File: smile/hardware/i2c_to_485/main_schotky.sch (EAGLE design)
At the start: 12 parts, among them IC1 MAX481CSA, IC2 MAX481CSA, U1 7402D

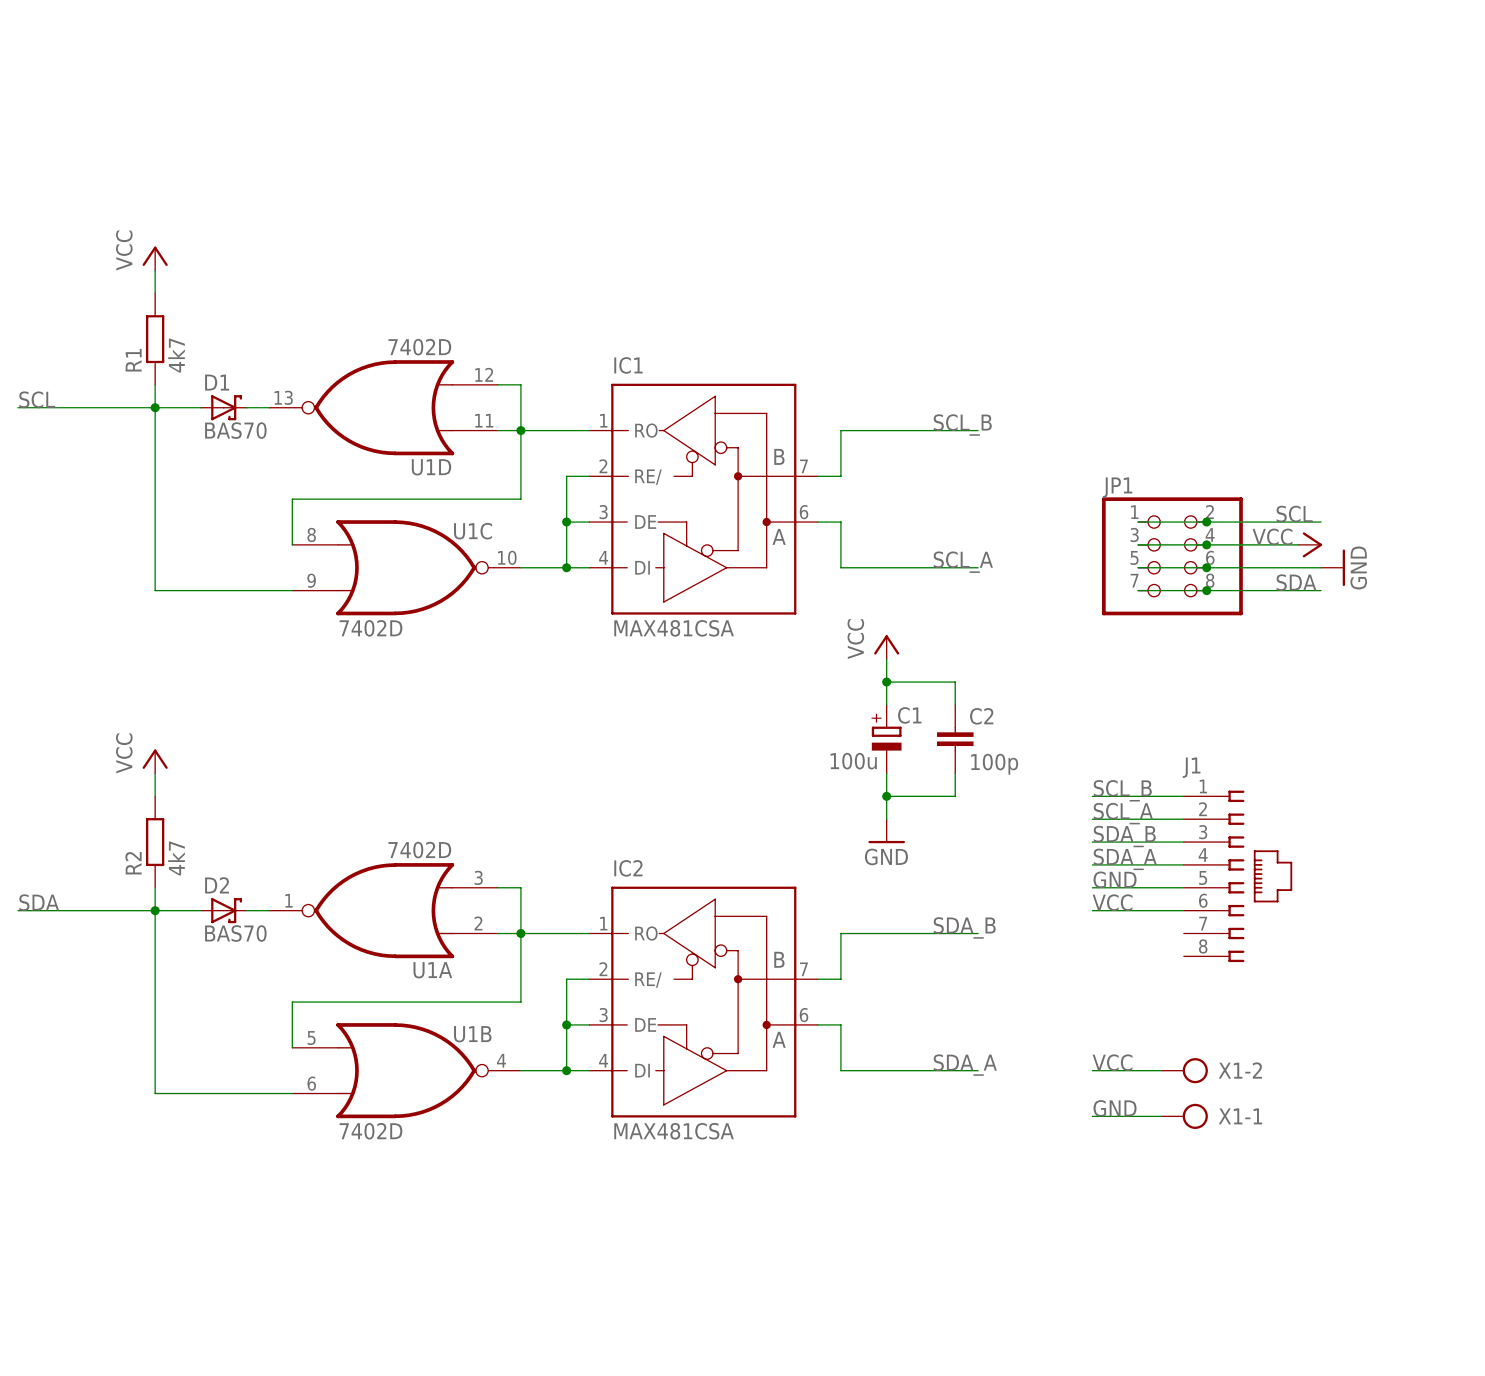
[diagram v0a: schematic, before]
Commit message: i2c to RS485 updated
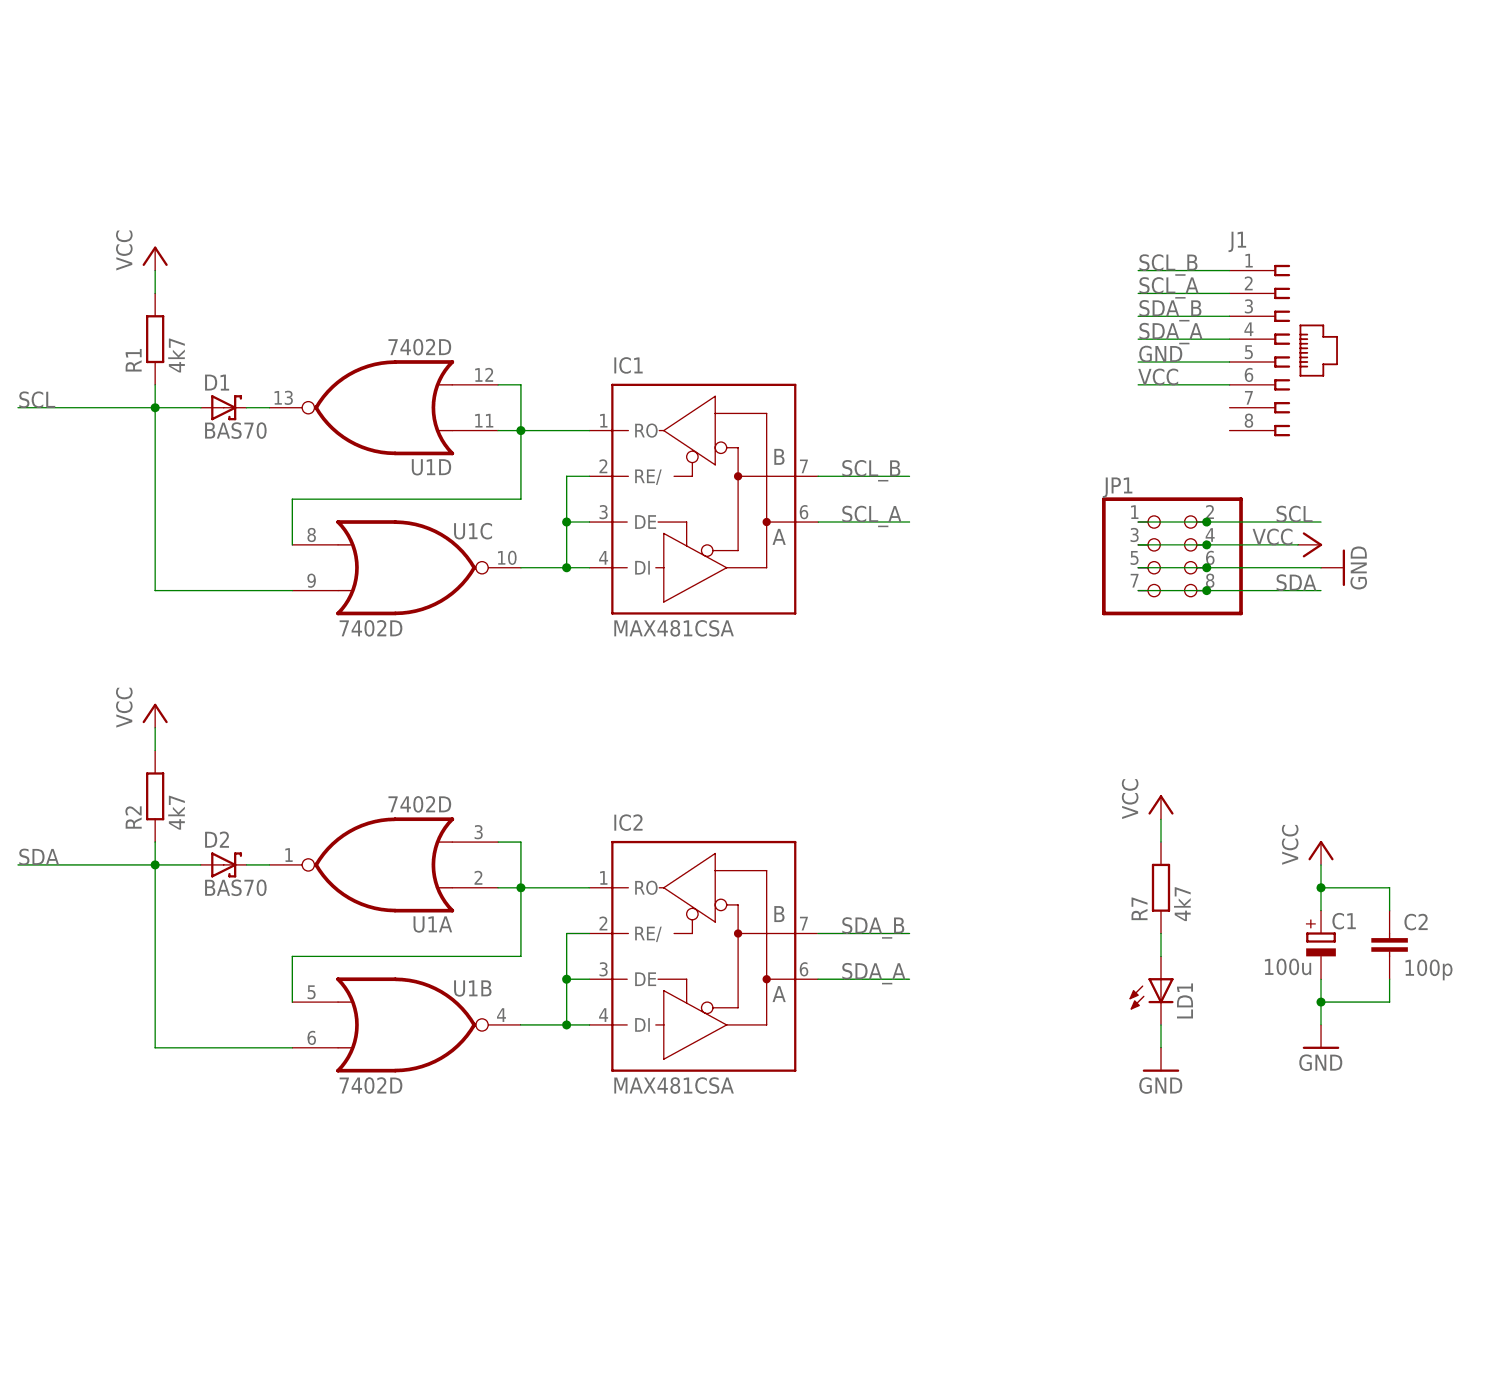
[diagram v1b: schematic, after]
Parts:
- removed X1: (no value), con-ptr500:AK500/2
- added LD1: (no value), led:LEDSMT1206
- added R7: 4k7, resistor:R-EU_R0805
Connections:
- new net N$5: LD1.A, R7.1
- net GND: now also LD1.C; no longer X1-1.KL
- net VCC: now also R7.2; no longer X1-2.KL
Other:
- moved on the sheet: C1, C2, D2, IC2, J1, R2, U1A, U1B

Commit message: i2c to rs485 - testing version
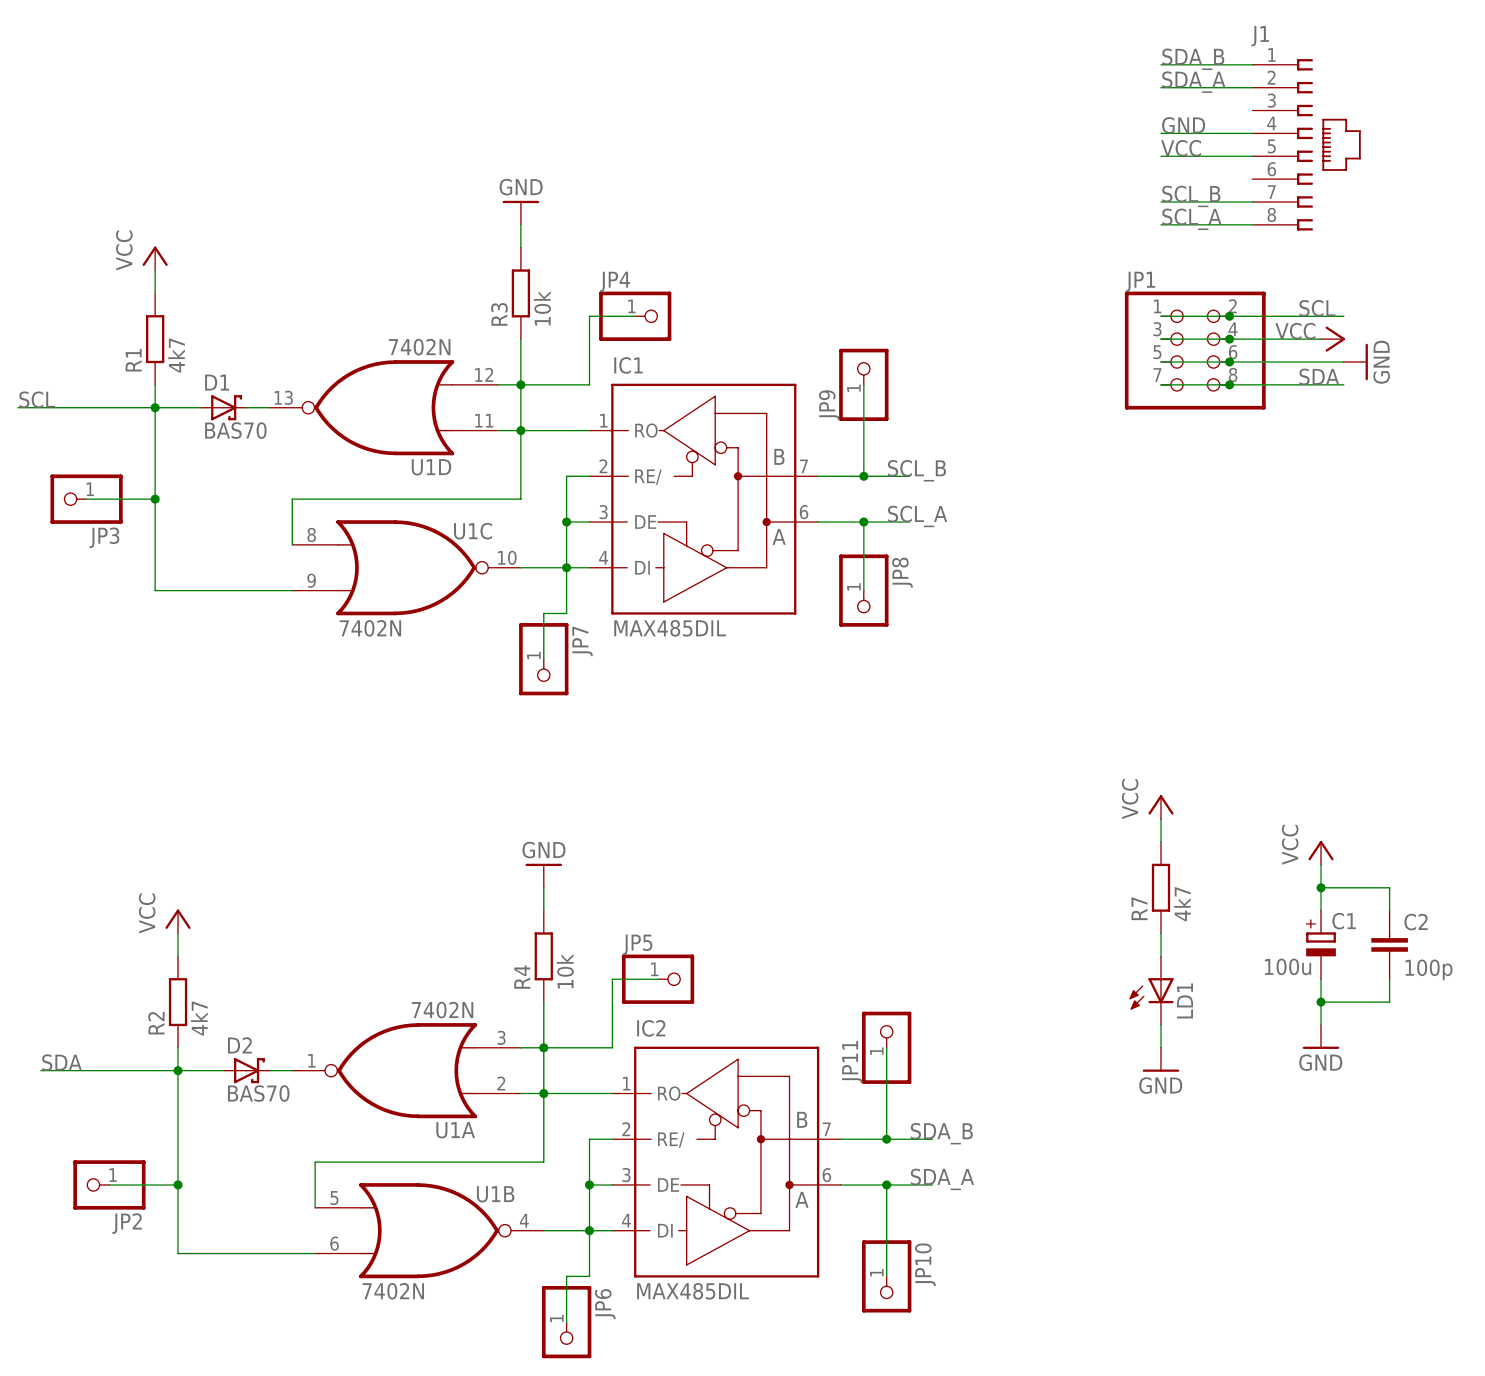
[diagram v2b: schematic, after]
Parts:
- added JP10, JP11, JP2, JP3, JP4, JP5, JP6, JP7, JP8, JP9: (no value), pinhead_v2:PINHD-1X1/LONG
- added R3, R4: 10k, resistor:R-EU_R0805
- IC1, IC2: value MAX481CSA -> MAX485DIL; device maxim:MAX481CSA -> maxim:MAX485DIL
- U1: value 7402D -> 7402N; device 74xx-us:7402D -> 74xx-us:7402N
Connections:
- net GND: now also J1.4, R3.2, R4.2; no longer J1.5
- net N$1: now also JP6.1
- net N$2: now also JP5.1, R4.1
- net N$6: now also JP7.1
- net N$7: now also JP4.1, R3.1
- net SCL: now also JP3.1
- net SCL_A: now also J1.8, JP8.1; no longer J1.2
- net SCL_B: now also J1.7, JP9.1; no longer J1.1
- net SDA: now also JP2.1
- net SDA_A: now also J1.2, JP10.1; no longer J1.4
- net SDA_B: now also J1.1, JP11.1; no longer J1.3
- net VCC: now also J1.5; no longer J1.6
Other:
- moved on the sheet: D2, IC2, J1, JP1, R2, U1A, U1B
